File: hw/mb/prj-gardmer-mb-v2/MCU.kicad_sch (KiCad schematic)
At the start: 31 parts, among them J1 Conn_01x05, Q9 BC817, SW1 Reset_SW, SW10 Unlock_SW, U1 PIC18F25Q10, U2 PCF8523T, Y1 8MHz, Y2 32.768kHz

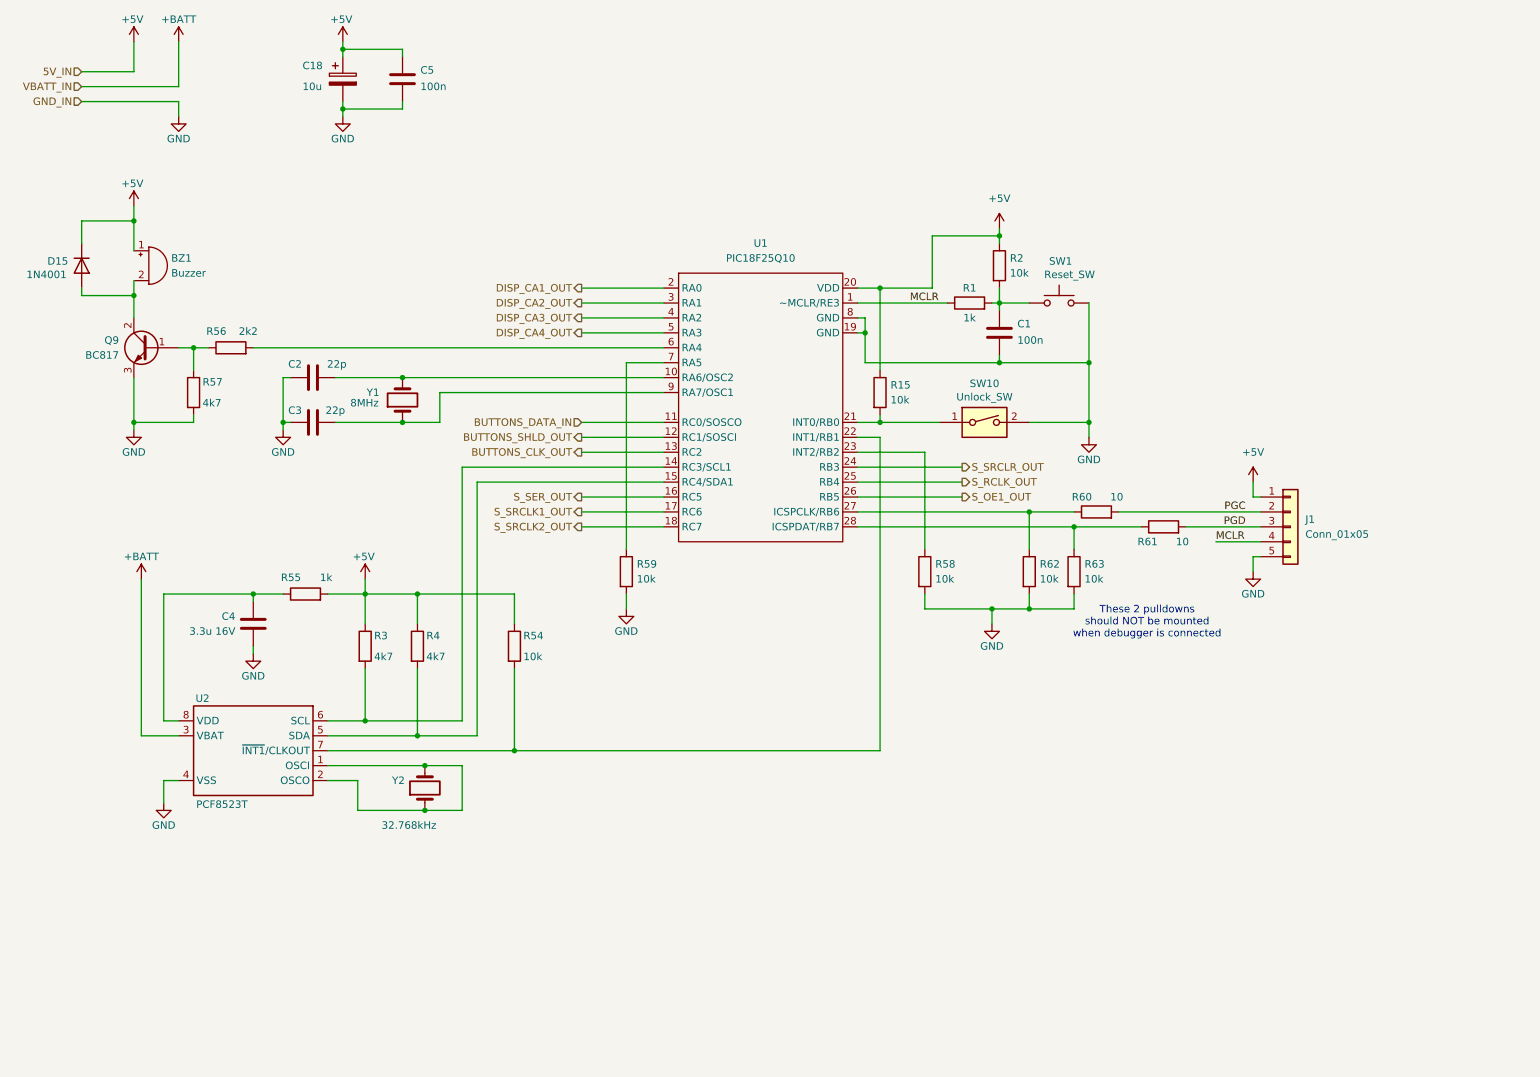
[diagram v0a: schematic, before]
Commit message: Added footprints and bom. Updated schematics.
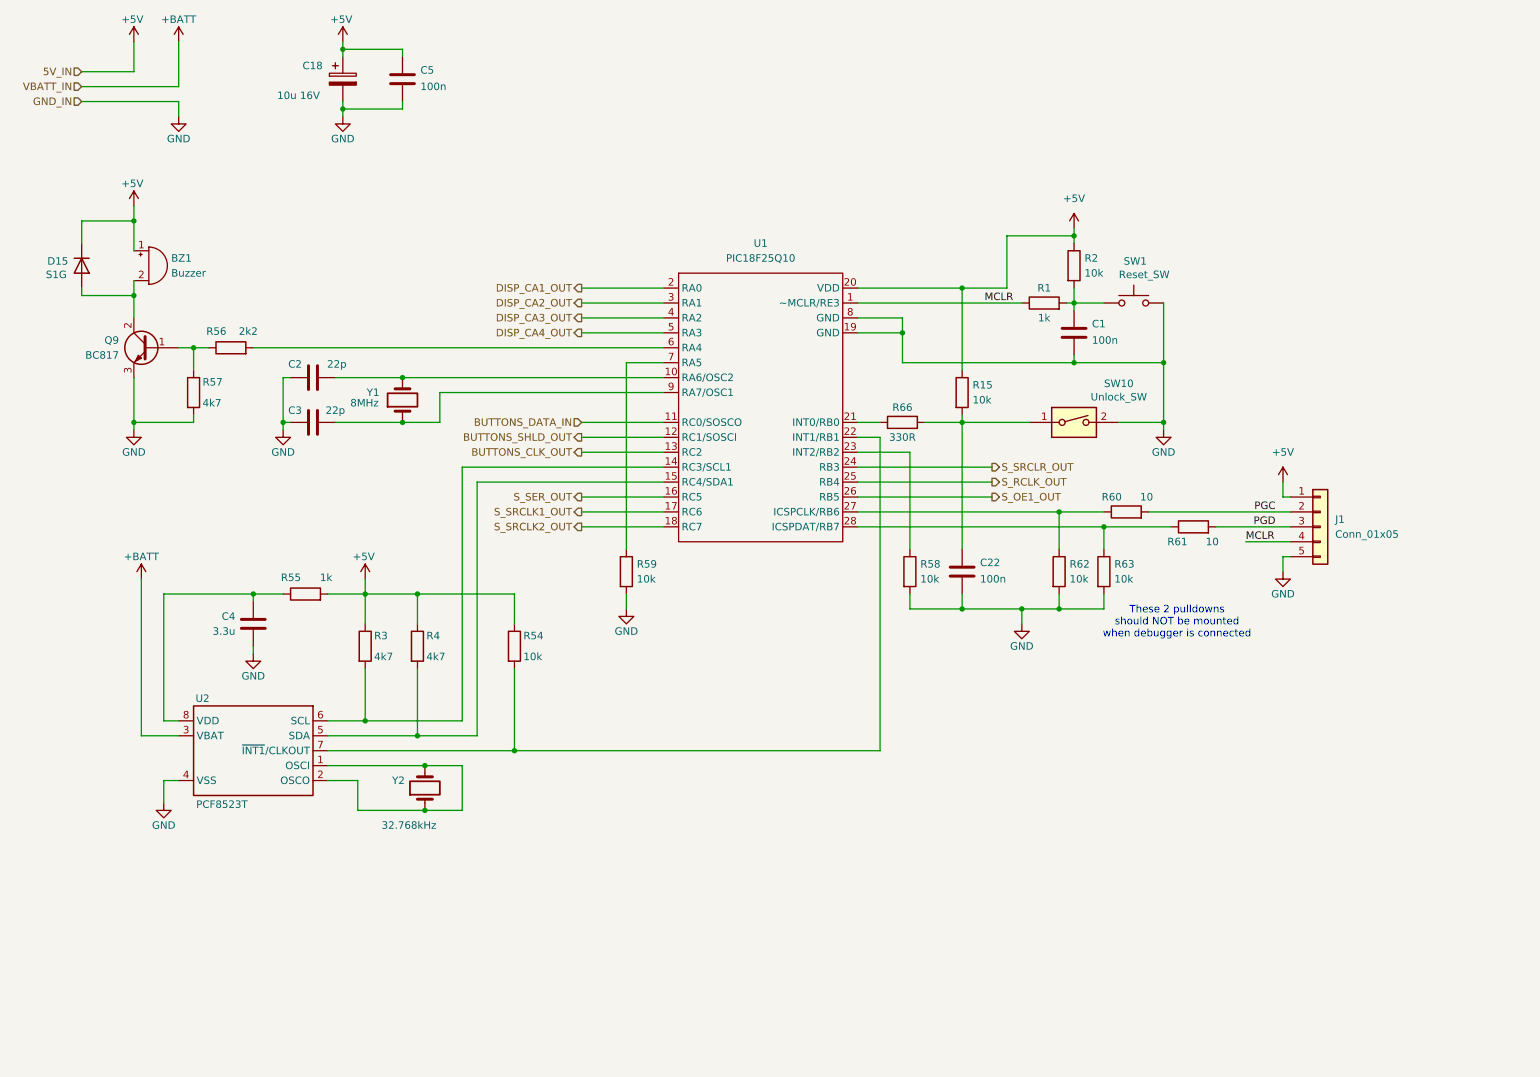
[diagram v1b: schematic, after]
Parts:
- added C22: 100n, symbol alf64:C
- added R66: 330R, symbol alf64:R
- C18: value 10u -> 10u 16V
- C4: value 3.3u 16V -> 3.3u
- D15: value 1N4001 -> S1G
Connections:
- net GND: now also C22.2
- net at R15.2, SW10.1: now also C22.1, R66.2; no longer U1.21 (INT0/RB0)
- new net: R66.1, U1.21 (INT0/RB0)
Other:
- moved on the sheet: C1, J1, R1, R15, R2, R58, R60, R61, R62, R63, SW1, SW10

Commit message: Assigned footprints to schematic symbols.
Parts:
- BZ1: footprint (none) -> alf64:Buzzer_THT_9.6mm
- C1, C2, C22, C3, C4, C5, R1, R15, R2, R3, R4, R54, R55, R56, R57, R58, R59, R60, R61, R62, R63, R66: footprint (none) -> alf64:Generic_0805
- C18: footprint (none) -> alf64:C_Tantal_1206
- D15: footprint (none) -> alf64:D_SMA
- J1: footprint (none) -> alf64:PinHeader_1x05_P2.54mm_Vertical
- Q9: footprint (none) -> alf64:SOT-23-3
- SW1: footprint (none) -> alf64:SW_PUSH_6mm
- SW10: footprint (none) -> alf64:Mss-2235s-sliderswitch
- U1: footprint (none) -> alf64:SOIC-28W_7.5x17.9mm_P1.27mm
- U2: footprint Package_SO:SOIC-8_3.9x4.9mm_P1.27mm -> alf64:SO-8_3.9x4.9mm_P1.27mm
- Y1: footprint (none) -> alf64:Crystal_HC49-U_Vertical
- Y2: footprint (none) -> alf64:Crystal_DS26_D2.0mm_L6.0mm_Horizontal
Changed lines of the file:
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@@
 			)
 		)
-		(property "Footprint" ""
+		(property "Footprint" "alf64:Generic_0805"
 			(at 53.34 74.168 90)
 			(effects
@@
 			)
 		)
-		(property "Footprint" ""
+		(property "Footprint" "alf64:SOIC-28W_7.5x17.9mm_P1.27mm"
 			(at 143.51 53.34 0)
 			(effects
@@
 			)
 		)
-		(property "Footprint" ""
+		(property "Footprint" "alf64:Generic_0805"
 			(at 167.64 86.868 90)
 			(effects
@@
 			)
 		)
-		(property "Footprint" ""
+		(property "Footprint" "alf64:SOT-23-3"
 			(at 34.29 69.85 0)
 			(effects
@@
 			)
 		)
-		(property "Footprint" ""
+		(property "Footprint" "alf64:Crystal_HC49-U_Vertical"
 			(at 82.55 81.28 0)
 			(effects
@@
 			)
 		)
-		(property "Footprint" ""
+		(property "Footprint" "alf64:Generic_0805"
 			(at 167.132 110.49 90)
 			(effects
@@
 			)
 		)
-		(property "Footprint" ""
+		(property "Footprint" "alf64:Generic_0805"
 			(at 178.7652 114.3 0)
 			(effects
@@
 			)
 		)
-		(property "Footprint" ""
+		(property "Footprint" "alf64:Generic_0805"
 			(at 71.12 76.5048 0)
 			(effects
@@
 			)
 		)
-		(property "Footprint" ""
+		(property "Footprint" "alf64:Generic_0805"
 			(at 205.74 102.108 90)
 			(effects
@@
 			)
 		)
-		(property "Footprint" ""
+		(property "Footprint" "alf64:Generic_0805"
 			(at 176.022 80.01 90)
 			(effects
@@
 			)
 		)
-		(property "Footprint" ""
+		(property "Footprint" "alf64:Generic_0805"
 			(at 83.5152 30.48 0)
 			(effects
@@
 			)
 		)
-		(property "Footprint" ""
+		(property "Footprint" "alf64:Crystal_DS26_D2.0mm_L6.0mm_Horizontal"
 			(at 86.36 147.32 0)
 			(effects
@@
 			)
 		)
-		(property "Footprint" ""
+		(property "Footprint" "alf64:Generic_0805"
 			(at 118.872 110.49 90)
 			(effects
@@
 			)
 		)
-		(property "Footprint" ""
+		(property "Footprint" "alf64:Generic_0805"
 			(at 200.152 110.49 90)
 			(effects
@@
 			)
 		)
-		(property "Footprint" ""
+		(property "Footprint" "alf64:Generic_0805"
 			(at 74.422 123.19 90)
 			(effects
@@
 			)
 		)
-		(property "Footprint" ""
+		(property "Footprint" "alf64:Generic_0805"
 			(at 83.312 123.19 90)
 			(effects
@@
 			)
 		)
-		(property "Footprint" ""
+		(property "Footprint" "alf64:D_SMA"
 			(at 27.94 58.42 0)
 			(effects
@@
 			)
 		)
-		(property "Footprint" "Package_SO:SOIC-8_3.9x4.9mm_P1.27mm"
+		(property "Footprint" "alf64:SO-8_3.9x4.9mm_P1.27mm"
 			(at 36.83 149.86 0)
 			(effects
@@
 			)
 		)
-		(property "Footprint" ""
+		(property "Footprint" "alf64:Generic_0805"
 			(at 45.212 80.01 90)
 			(effects
@@
 			)
 		)
-		(property "Footprint" ""
+		(property "Footprint" "alf64:PinHeader_1x05_P2.54mm_Vertical"
 			(at 238.76 102.87 0)
 			(effects
@@
 			)
 		)
-		(property "Footprint" ""
+		(property "Footprint" "alf64:Generic_0805"
 			(at 71.12 84.1248 0)
 			(effects
@@
 			)
 		)
-		(property "Footprint" ""
+		(property "Footprint" "alf64:Generic_0805"
 			(at 217.17 104.648 90)
 			(effects
@@
 			)
 		)
-		(property "Footprint" ""
+		(property "Footprint" "alf64:Generic_0805"
 			(at 99.822 123.19 90)
 			(effects
@@
 			)
 		)
-		(property "Footprint" ""
+		(property "Footprint" "alf64:C_Tantal_1206"
 			(at 73.3552 30.48 0)
 			(effects
@@
 			)
 		)
-		(property "Footprint" ""
+		(property "Footprint" "alf64:SW_PUSH_6mm"
 			(at 207.01 59.69 0)
 			(effects
@@
 			)
 		)
-		(property "Footprint" ""
+		(property "Footprint" "alf64:Generic_0805"
 			(at 195.072 58.42 90)
 			(effects
@@
 			)
 		)
-		(property "Footprint" ""
+		(property "Footprint" "alf64:Generic_0805"
 			(at 66.04 116.078 90)
 			(effects
@@
 			)
 		)
-		(property "Footprint" ""
+		(property "Footprint" "alf64:Mss-2235s-sliderswitch"
 			(at 196.85 85.09 0)
 			(effects
@@
 			)
 		)
-		(property "Footprint" ""
+		(property "Footprint" "alf64:Buzzer_THT_9.6mm"
 			(at 38.735 55.88 90)
 			(effects
@@
 			)
 		)
-		(property "Footprint" ""
+		(property "Footprint" "alf64:Generic_0805"
 			(at 56.1848 123.19 0)
 			(effects
@@
 			)
 		)
-		(property "Footprint" ""
+		(property "Footprint" "alf64:Generic_0805"
 			(at 192.532 110.49 90)
 			(effects
@@
 			)
 		)
-		(property "Footprint" ""
+		(property "Footprint" "alf64:Generic_0805"
 			(at 191.77 66.548 90)
 			(effects
@@
 			)
 		)
-		(property "Footprint" ""
+		(property "Footprint" "alf64:Generic_0805"
 			(at 197.8152 73.66 0)
 			(effects

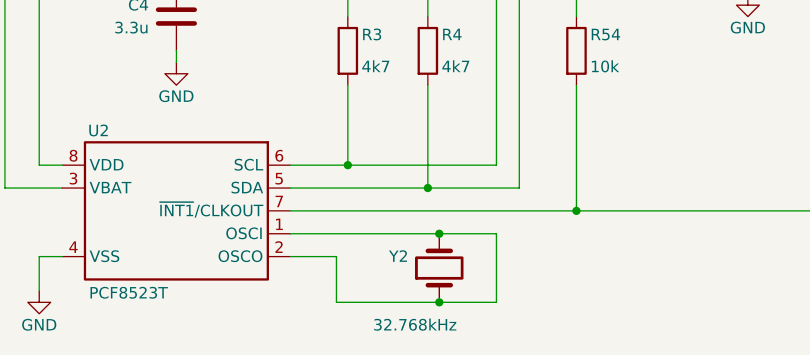
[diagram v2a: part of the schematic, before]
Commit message: Updated schematic: - added test points instead of connections between relays and outputs - fixed crystal connection for rtc
Updated PCB:
- halfway through the routing

Updated footprints:
- added footprints for test points
- reduced size of pads for D_SMA
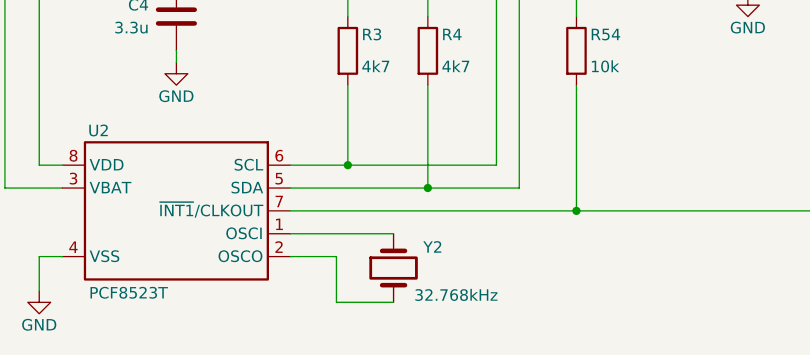
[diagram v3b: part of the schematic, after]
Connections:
- net at U2.1 (OSCI), Y2.1: no longer U2.2 (OSCO), Y2.2
- new net: U2.2 (OSCO), Y2.2
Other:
- moved on the sheet: Y2
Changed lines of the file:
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@@
-	)
-	(junction
-		(at 86.36 143.51)
-		(diameter 0)
-		(color 0 0 0 0)
 	)
 	(junction
@@
 	)
 	(junction
-		(at 86.36 151.13)
-		(diameter 0)
-		(color 0 0 0 0)
-	)
-	(junction
 		(at 177.8 85.09)
 		(diameter 0)
@@
 	(wire
 		(pts
-			(xy 86.36 143.51) (xy 92.71 143.51)
-		)
-		(stroke
-			(width 0)
-			(type default)
-		)
-	)
-	(wire
-		(pts
 			(xy 27.94 27.94) (xy 44.45 27.94)
 		)
@@
 	(wire
 		(pts
-			(xy 92.71 151.13) (xy 92.71 143.51)
-		)
-		(stroke
-			(width 0)
-			(type default)
-		)
-	)
-	(wire
-		(pts
 			(xy 113.03 102.87) (xy 127 102.87)
 		)
@@
 	(wire
 		(pts
-			(xy 69.85 143.51) (xy 86.36 143.51)
+			(xy 69.85 143.51) (xy 81.28 143.51)
 		)
 		(stroke
@@
 	(wire
 		(pts
-			(xy 74.93 151.13) (xy 86.36 151.13)
-		)
-		(stroke
-			(width 0)
-			(type default)
-		)
-	)
-	(wire
-		(pts
-			(xy 86.36 151.13) (xy 92.71 151.13)
+			(xy 74.93 151.13) (xy 81.28 151.13)
 		)
 		(stroke
@@
 	(symbol
 		(lib_id "alf64:Crystal")
-		(at 86.36 147.32 90)
+		(at 81.28 147.32 90)
+		(mirror x)
 		(unit 1)
 		(exclude_from_sim no)
@@
 		(dnp no)
 		(property "Reference" "Y2"
-			(at 80.772 146.05 90)
+			(at 84.582 145.034 90)
 			(effects
 				(font
@@
 		)
 		(property "Value" "32.768kHz"
-			(at 78.994 153.67 90)
+			(at 83.566 150.368 90)
 			(effects
 				(font
@@
 		)
 		(property "Footprint" "alf64:Crystal_DS26_D2.0mm_L6.0mm_Horizontal"
-			(at 86.36 147.32 0)
+			(at 81.28 147.32 0)
 			(effects
 				(font
@@
 		)
 		(property "Datasheet" "~"
-			(at 86.36 147.32 0)
+			(at 81.28 147.32 0)
 			(effects
 				(font
@@
 		)
 		(property "Description" "Two pin crystal"
-			(at 86.36 147.32 0)
-			(effects
-				(font
+			(at 81.28 147.32 0)
+			(effects
+				(font

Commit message: Updated schematic (footprints assign), PCB and footprints: - Changed the 'Generic' footprints that were used for capacitors, resistors and fuses into specific ones (I.e. Generic_0805 is replaced by C_0805 and R_0805). - Differentiated the D_0805 and LED_0805 footprints
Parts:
- C1, C2, C22, C3, C4, C5: footprint alf64:Generic_0805 -> alf64:C_0805
- R1, R15, R2, R3, R4, R54, R55, R56, R57, R58, R59, R60, R61, R62, R63, R66: footprint alf64:Generic_0805 -> alf64:R_0805
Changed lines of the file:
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@@
 			)
 		)
-		(property "Footprint" "alf64:Generic_0805"
+		(property "Footprint" "alf64:R_0805"
 			(at 53.34 74.168 90)
 			(effects
@@
 			)
 		)
-		(property "Footprint" "alf64:Generic_0805"
+		(property "Footprint" "alf64:R_0805"
 			(at 167.64 86.868 90)
 			(effects
@@
 			)
 		)
-		(property "Footprint" "alf64:Generic_0805"
+		(property "Footprint" "alf64:R_0805"
 			(at 167.132 110.49 90)
 			(effects
@@
 			)
 		)
-		(property "Footprint" "alf64:Generic_0805"
+		(property "Footprint" "alf64:C_0805"
 			(at 178.7652 114.3 0)
 			(effects
@@
 			)
 		)
-		(property "Footprint" "alf64:Generic_0805"
+		(property "Footprint" "alf64:C_0805"
 			(at 71.12 76.5048 0)
 			(effects
@@
 			)
 		)
-		(property "Footprint" "alf64:Generic_0805"
+		(property "Footprint" "alf64:R_0805"
 			(at 205.74 102.108 90)
 			(effects
@@
 			)
 		)
-		(property "Footprint" "alf64:Generic_0805"
+		(property "Footprint" "alf64:R_0805"
 			(at 176.022 80.01 90)
 			(effects
@@
 			)
 		)
-		(property "Footprint" "alf64:Generic_0805"
+		(property "Footprint" "alf64:C_0805"
 			(at 83.5152 30.48 0)
 			(effects
@@
 			)
 		)
-		(property "Footprint" "alf64:Generic_0805"
+		(property "Footprint" "alf64:R_0805"
 			(at 118.872 110.49 90)
 			(effects
@@
 			)
 		)
-		(property "Footprint" "alf64:Generic_0805"
+		(property "Footprint" "alf64:R_0805"
 			(at 200.152 110.49 90)
 			(effects
@@
 			)
 		)
-		(property "Footprint" "alf64:Generic_0805"
+		(property "Footprint" "alf64:R_0805"
 			(at 74.422 123.19 90)
 			(effects
@@
 			)
 		)
-		(property "Footprint" "alf64:Generic_0805"
+		(property "Footprint" "alf64:R_0805"
 			(at 83.312 123.19 90)
 			(effects
@@
 			)
 		)
-		(property "Footprint" "alf64:Generic_0805"
+		(property "Footprint" "alf64:R_0805"
 			(at 45.212 80.01 90)
 			(effects
@@
 			)
 		)
-		(property "Footprint" "alf64:Generic_0805"
+		(property "Footprint" "alf64:C_0805"
 			(at 71.12 84.1248 0)
 			(effects
@@
 			)
 		)
-		(property "Footprint" "alf64:Generic_0805"
+		(property "Footprint" "alf64:R_0805"
 			(at 217.17 104.648 90)
 			(effects
@@
 			)
 		)
-		(property "Footprint" "alf64:Generic_0805"
+		(property "Footprint" "alf64:R_0805"
 			(at 99.822 123.19 90)
 			(effects
@@
 			)
 		)
-		(property "Footprint" "alf64:Generic_0805"
+		(property "Footprint" "alf64:R_0805"
 			(at 195.072 58.42 90)
 			(effects
@@
 			)
 		)
-		(property "Footprint" "alf64:Generic_0805"
+		(property "Footprint" "alf64:R_0805"
 			(at 66.04 116.078 90)
 			(effects
@@
 			)
 		)
-		(property "Footprint" "alf64:Generic_0805"
+		(property "Footprint" "alf64:C_0805"
 			(at 56.1848 123.19 0)
 			(effects
@@
 			)
 		)
-		(property "Footprint" "alf64:Generic_0805"
+		(property "Footprint" "alf64:R_0805"
 			(at 192.532 110.49 90)
 			(effects
@@
 			)
 		)
-		(property "Footprint" "alf64:Generic_0805"
+		(property "Footprint" "alf64:R_0805"
 			(at 191.77 66.548 90)
 			(effects
@@
 			)
 		)
-		(property "Footprint" "alf64:Generic_0805"
+		(property "Footprint" "alf64:C_0805"
 			(at 197.8152 73.66 0)
 			(effects

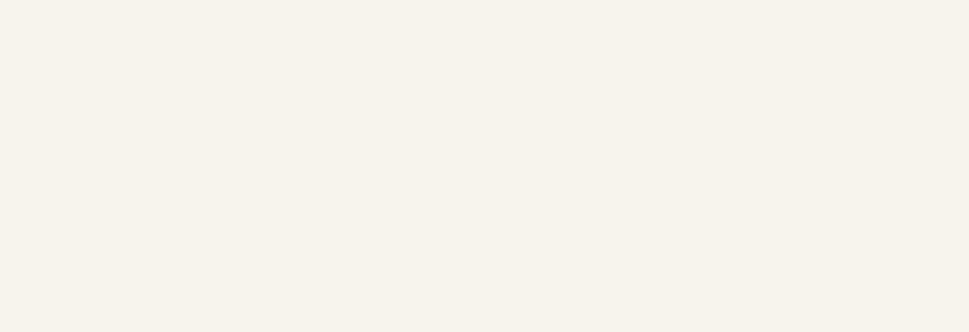
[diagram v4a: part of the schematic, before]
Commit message: Updated the hw release of prj-gardmer-mb-v2 rev001: - reorganized files in catalogues - added schematic in .pdf - added top & bottom elements on pcb in .pdf - added bom
Updated schematic:
- added a title, rev and date to the drawing info table on each sheet
- excluded test points ('TP' elements) from BOM

Updated PCB:
- added a title, rev and date to the drawing info table
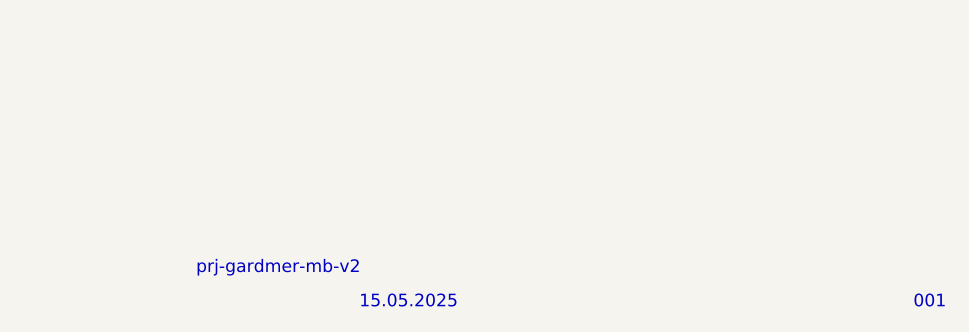
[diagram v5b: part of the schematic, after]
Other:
- note added: "001"
- note added: "15.05.2025"
- note added: "prj-gardmer-mb-v2"
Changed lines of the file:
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@@
+		)
+	)
+	(text "prj-gardmer-mb-v2"
+		(exclude_from_sim no)
+		(at 199.39 189.484 0)
+		(effects
+			(font
+				(size 1.397 1.397)
+			)
+		)
+	)
+	(text "15.05.2025"
+		(exclude_from_sim no)
+		(at 213.868 193.294 0)
+		(effects
+			(font
+				(size 1.397 1.397)
+			)
+		)
+	)
+	(text "001"
+		(exclude_from_sim no)
+		(at 271.78 193.294 0)
+		(effects
+			(font
+				(size 1.397 1.397)
+			)
 		)
 	)
